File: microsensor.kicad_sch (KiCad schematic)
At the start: 24 parts, among them J1 ARM SWD, SW1 Control, U1 BMD-360-A-R, U2 RV-3028-C7, U3 HDC2080

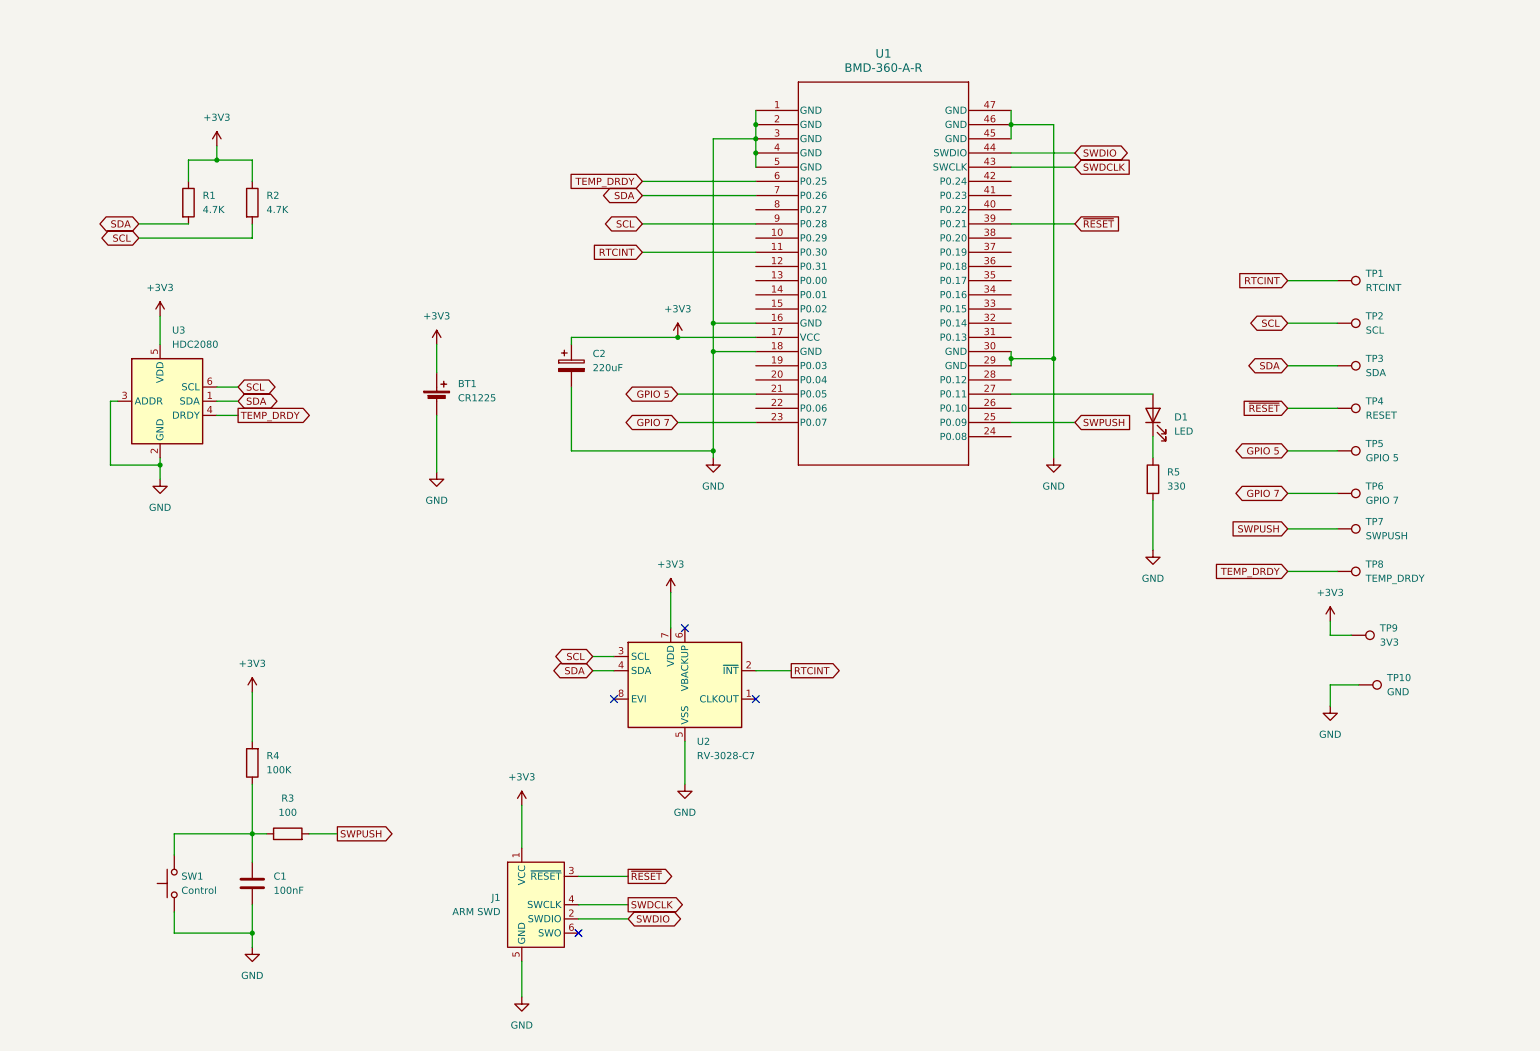
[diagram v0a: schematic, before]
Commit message: Shrink to 45x35 Unify R sizes to 0805 Rearrange Add dimensions (User layer)
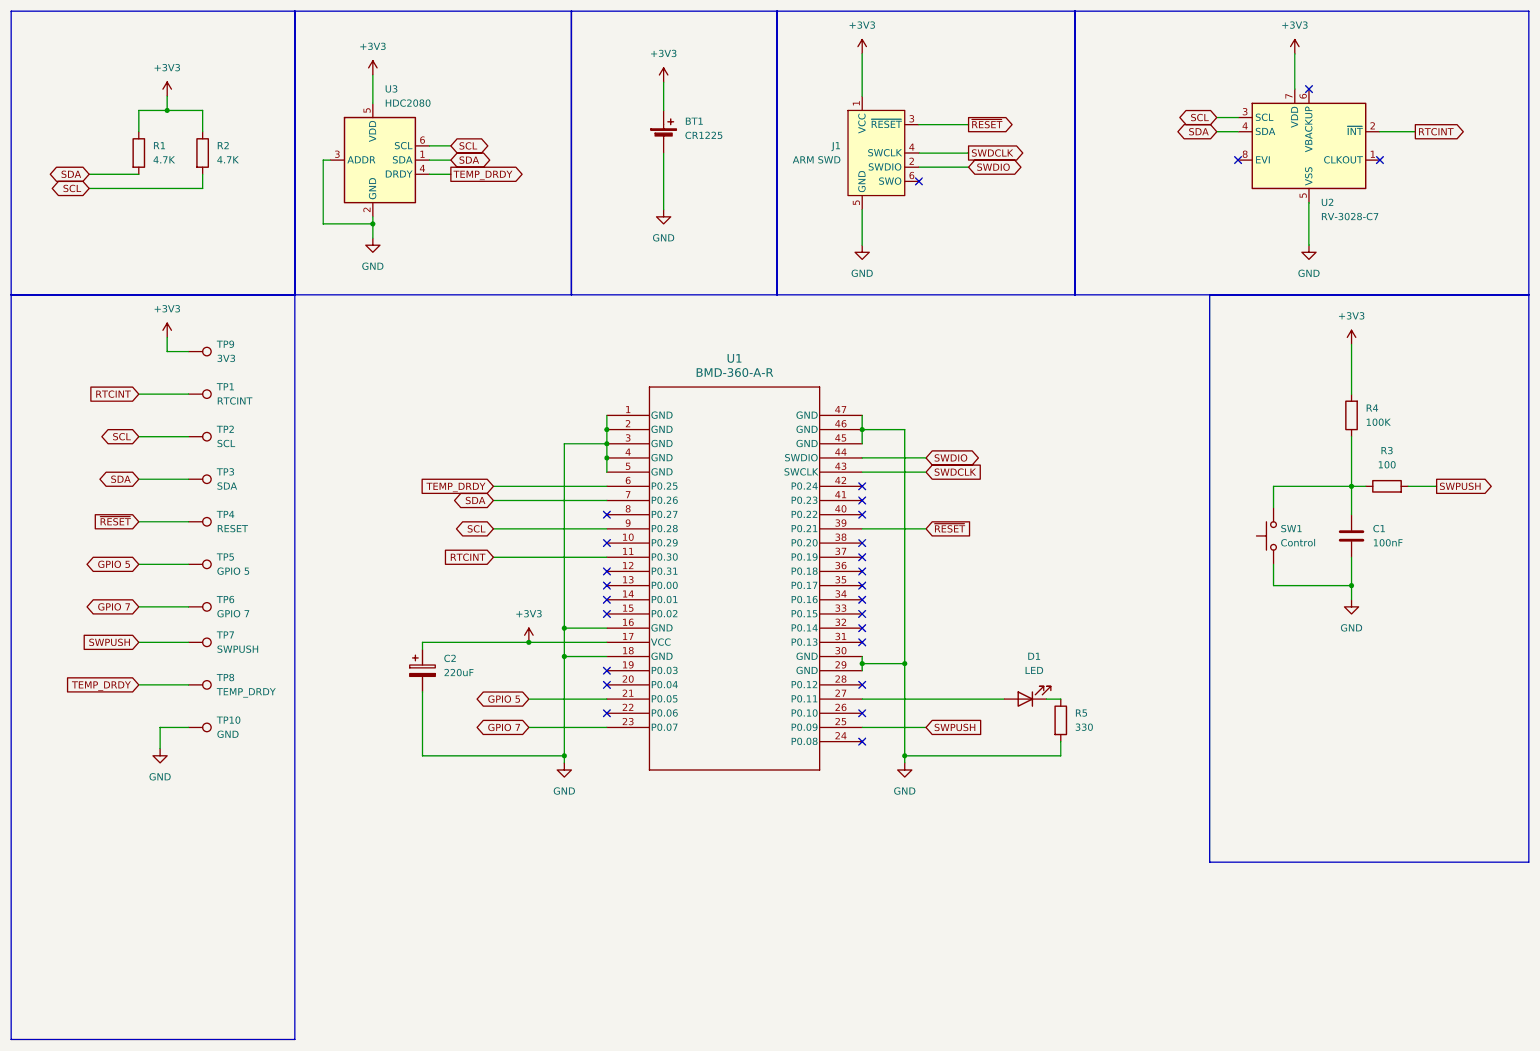
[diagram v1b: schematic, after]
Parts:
- R3, R4: footprint Resistor_SMD:R_1206_3216Metric -> Resistor_SMD:R_0805_2012Metric
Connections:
- no-connect marks 4 -> 27
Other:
- moved on the sheet: BT1, C1, C2, D1, J1, R1, R2, R3, R4, R5, SW1, TP1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

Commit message: Added bom related properties
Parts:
- TP1, TP10, TP2, TP3, TP4, TP5, TP6, TP7, TP8, TP9: now left out of the parts list
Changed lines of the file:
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@@
 		(unit 1)
 		(exclude_from_sim no)
-		(in_bom yes)
+		(in_bom no)
 		(on_board yes)
 		(dnp no)
@@
 		(unit 1)
 		(exclude_from_sim no)
-		(in_bom yes)
+		(in_bom no)
 		(on_board yes)
 		(dnp no)
@@
 		(unit 1)
 		(exclude_from_sim no)
-		(in_bom yes)
+		(in_bom no)
 		(on_board yes)
 		(dnp no)
@@
 		(unit 1)
 		(exclude_from_sim no)
-		(in_bom yes)
+		(in_bom no)
 		(on_board yes)
 		(dnp no)
@@
 		(unit 1)
 		(exclude_from_sim no)
-		(in_bom yes)
+		(in_bom no)
 		(on_board yes)
 		(dnp no)
@@
 		(unit 1)
 		(exclude_from_sim no)
-		(in_bom yes)
+		(in_bom no)
 		(on_board yes)
 		(dnp no)
@@
 		(unit 1)
 		(exclude_from_sim no)
-		(in_bom yes)
+		(in_bom no)
 		(on_board yes)
 		(dnp no)
@@
 		(unit 1)
 		(exclude_from_sim no)
-		(in_bom yes)
+		(in_bom no)
 		(on_board yes)
 		(dnp no)
@@
 		(unit 1)
 		(exclude_from_sim no)
-		(in_bom yes)
+		(in_bom no)
 		(on_board yes)
 		(dnp no)
@@
 		(unit 1)
 		(exclude_from_sim no)
-		(in_bom yes)
-		(on_board yes)
-		(dnp no)
+		(in_bom no)
+		(on_board yes)
+		(dnp no)

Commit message: Smaller version 25mmx25mm
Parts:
- removed C2: 220uF, Capacitor_Tantalum_SMD:CP_EIA-3528-21_Kemet-B, symbol Device:C_Polarized
- removed TP1: RTCINT, TestPoint:TestPoint_Pad_D1.0mm, symbol Connector:TestPoint
- removed TP10: GND, TestPoint:TestPoint_Pad_D1.0mm, symbol Connector:TestPoint
- removed TP2: SCL, TestPoint:TestPoint_Pad_D1.0mm, symbol Connector:TestPoint
- removed TP3: SDA, TestPoint:TestPoint_Pad_D1.0mm, symbol Connector:TestPoint
- removed TP4: RESET, TestPoint:TestPoint_Pad_D1.0mm, symbol Connector:TestPoint
- removed TP5: GPIO 5, TestPoint:TestPoint_Pad_D1.0mm, symbol Connector:TestPoint
- removed TP6: GPIO 7, TestPoint:TestPoint_Pad_D1.0mm, symbol Connector:TestPoint
- removed TP7: SWPUSH, TestPoint:TestPoint_Pad_D1.0mm, symbol Connector:TestPoint
- removed TP8: TEMP_DRDY, TestPoint:TestPoint_Pad_D1.0mm, symbol Connector:TestPoint
- removed TP9: 3V3, TestPoint:TestPoint_Pad_D1.0mm, symbol Connector:TestPoint
- added C2: 220uF, Capacitor_SMD:C_1206_3216Metric, symbol Device:C
- added R6: 100, Resistor_SMD:R_0805_2012Metric, symbol Device:R
- C1: footprint Capacitor_SMD:C_1206_3216Metric -> Capacitor_SMD:C_0805_2012Metric
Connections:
- net +3V3: now also C2.1, R6.2; no longer BT1.1 (+)
- net GND: now also C2.2
- net SWPUSH: now also U1.31 (P0.13); no longer U1.25 (P0.09)
- new net +BAT: BT1.1 (+), R6.1
- no-connect marks 27 -> 26
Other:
- moved on the sheet: BT1

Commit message: Change battery holder, update layout
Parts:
- BT1: footprint Battery:BatteryHolder_Keystone_3000_1x12mm -> footprints:Keystone 110 and 112 for CR20xx
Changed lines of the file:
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@@
 			)
 		)
-		(property "Footprint" "Battery:BatteryHolder_Keystone_3000_1x12mm"
+		(property "Footprint" "footprints:Keystone 110 and 112 for CR20xx"
 			(at 27.94 100.076 90)
 			(effects

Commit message: Switch to nRF54L15 (NORA B206)
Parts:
- removed U1: BMD-360-A-R, BMD-360_UBL, symbol BMD-360-A-R:BMD-360-A-R
- added C3: 100n, Capacitor_SMD:C_0805_2012Metric, symbol Device:C
- added U1: NORA B206, symbol NORA-B2x5:NORA-B2x6
- added Y1: 32768, Crystal:Crystal_SMD_2012-2Pin_2.0x1.2mm, symbol Device:Crystal
- R5: value 330 -> 100
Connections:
- net +3V3: now also C3.1, U1.A7 (Vdd), U1.A8 (Vdd), U1.B7 (Vdd)
- net GND: now also U2.8 (EVI), C3.2, U1.A1 (GND), U1.A9 (GND), U1.B2 (GND), U1.B8 (GND), U1.E4 (GND), U1.E5 (GND), U1.F4 (GND), U1.F5 (GND), U1.K2 (GND), U1.K3 (GND), U1.K5 (GND), U1.K7 (GND), U1.K8 (GND), U1.L1 (GND), U1.L9 (GND), U1.M1 (GND), U1.M2 (GND), U1.M8 (GND), U1.M9 (GND)
- net SCL: now also U1.H9 (P1.10)
- net SDA: now also U1.J9 (P0.03)
- net SWDCLK: now also U1.J2 (SWDCLK)
- net SWDIO: now also U1.H2 (SWDIO)
- net ~{RESET}: now also U1.J3 (~{RESET})
- net SWO: now reaches J1.6 (SWO)
- net SWO: now also U1.C4 (SWO)
- net LED: now reaches D1.2 (A)
- net LED: now also U1.B1 (P2.06)
- net RTCINT renamed ~{RTCINT}
- net ~{RTCINT}: now also U1.G9 (P1.05)
- net SWPUSH renamed ~{SWPUSH}
- net ~{SWPUSH}: now also U1.A3 (P1.11)
- net TEMP_DRDY renamed T_DRDY
- net T_DRDY: now also U1.E9 (P1.08)
- new net XL1: U1.B6 (P1.00), Y1.2
- new net XL2: U1.C6 (P1.01), Y1.1
- no-connect marks 26 -> 2
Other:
- moved on the sheet: J1, U2

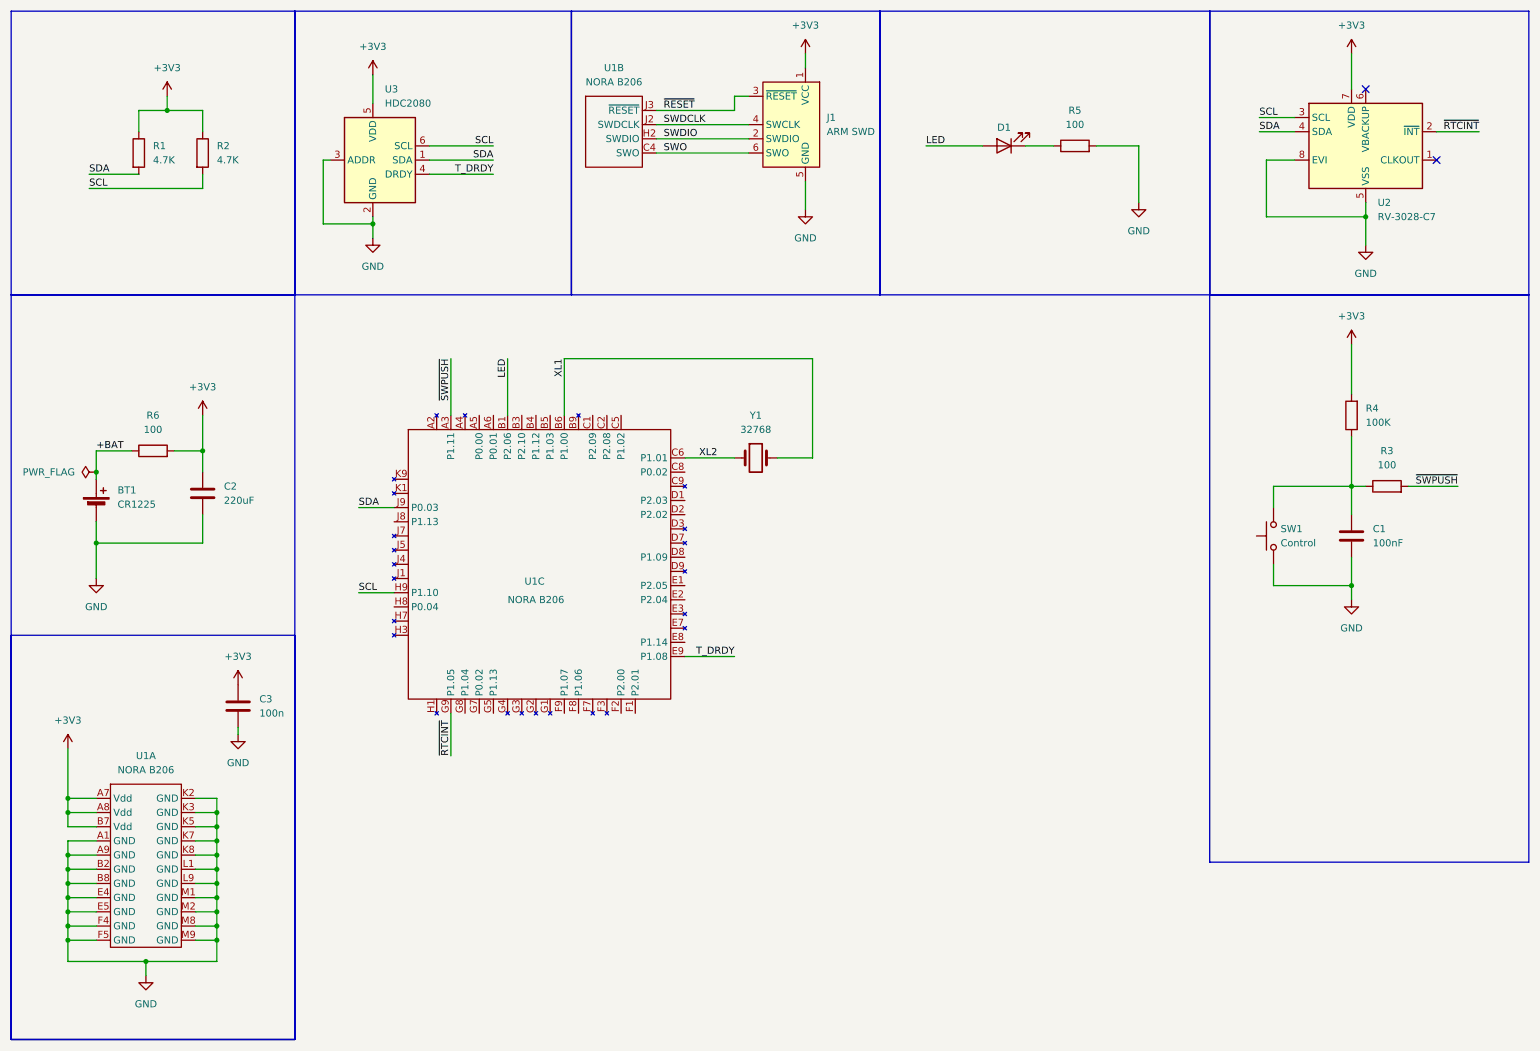
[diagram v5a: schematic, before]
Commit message: Finalize routing for NORA module Add and route VSENSE circuit
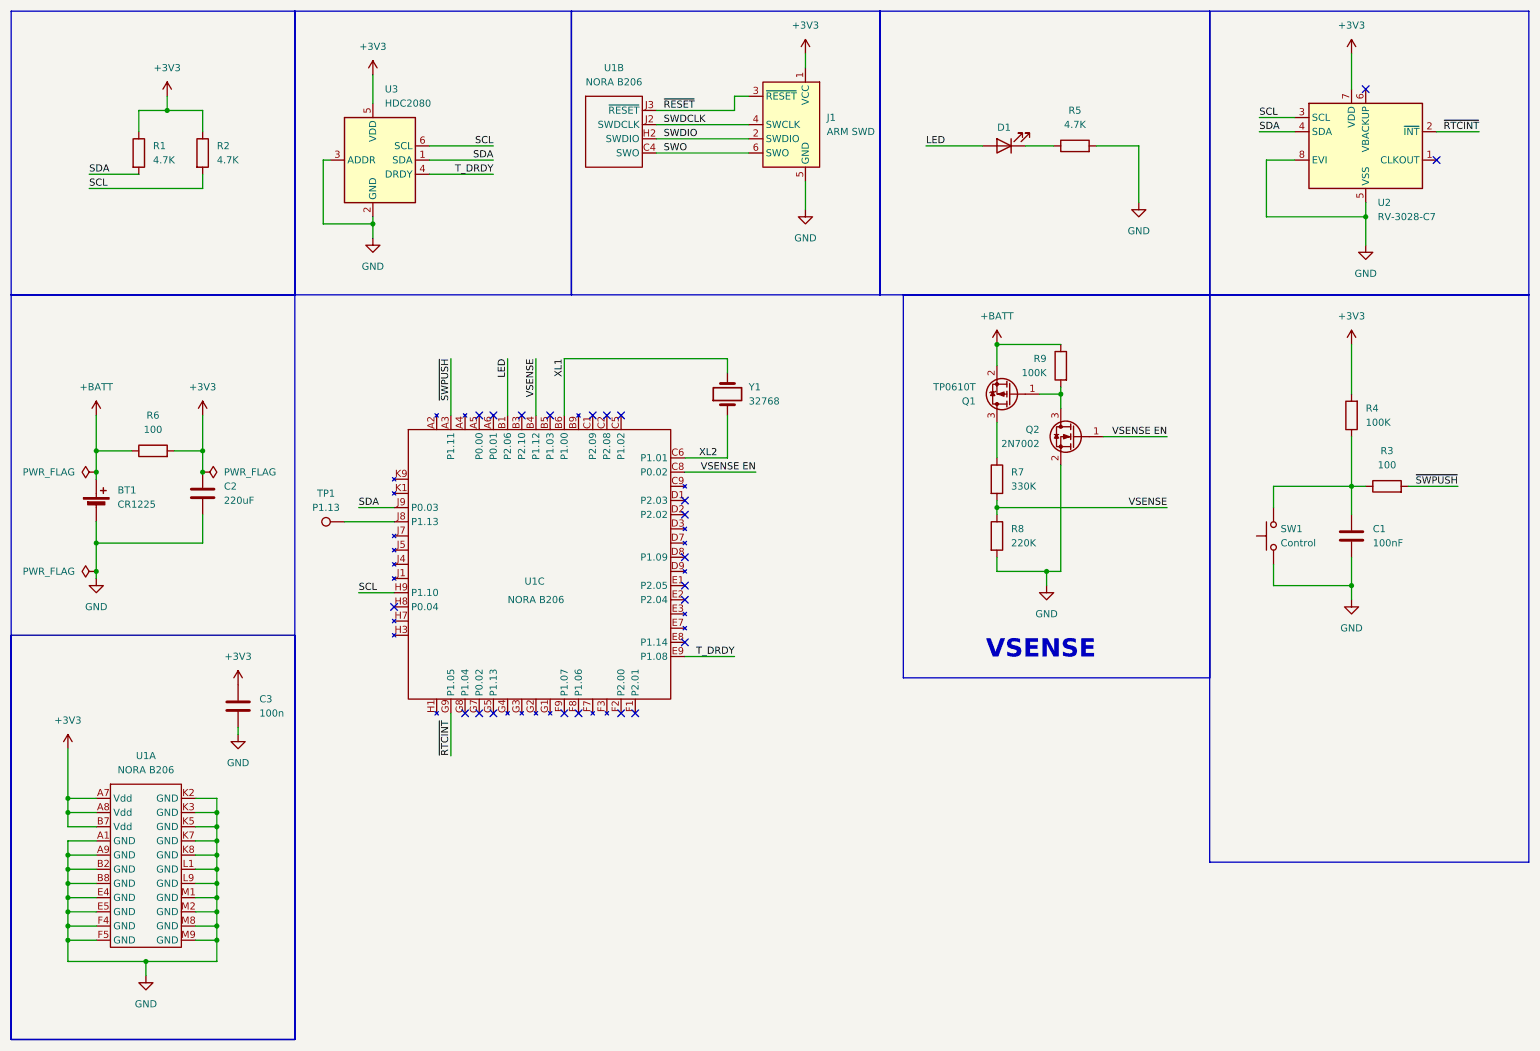
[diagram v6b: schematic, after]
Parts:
- added Q1: TP0610T, Package_TO_SOT_SMD:SOT-23, symbol Transistor_FET:TP0610T
- added Q2: 2N7002, Package_TO_SOT_SMD:SOT-23, symbol Transistor_FET:2N7002
- added R7: 330K, Resistor_SMD:R_0805_2012Metric, symbol Device:R
- added R8: 220K, Resistor_SMD:R_0805_2012Metric, symbol Device:R
- added R9: 100K, Resistor_SMD:R_0805_2012Metric, symbol Device:R
- added TP1: P1.13, TestPoint:TestPoint_Pad_1.5x1.5mm, symbol Connector:TestPoint
- R5: value 100 -> 4.7K
- U1: footprint (none) -> footprints:NORA-B2x6
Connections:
- net GND: now also Q2.2 (S), R8.2
- net VSENSE: now reaches U1.B4 (P1.12)
- net VSENSE: now also R7.2, R8.1
- net VSENSE EN: now reaches U1.C8 (P0.02)
- net VSENSE EN: now also Q2.1 (G)
- net at U1.J8 (P1.13): now also TP1.1
- net +BAT renamed +BATT
- net +BATT: now also Q1.2 (S), R9.1
- new net: Q1.3 (D), R7.1
- new net: Q1.1 (G), Q2.3 (D), R9.2
- no-connect marks 2 -> 23
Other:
- note added: "VSENSE"
- moved on the sheet: Y1

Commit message: v0.2 BOM + document with issues
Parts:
- TP1: now left out of the parts list
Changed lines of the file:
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@@
 		(unit 1)
 		(exclude_from_sim no)
-		(in_bom yes)
+		(in_bom no)
 		(on_board yes)
 		(dnp no)
